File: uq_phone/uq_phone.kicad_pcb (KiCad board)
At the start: 4 copper layers, 116.9 x 105 mm, 171 parts, among them J1 USB4105-GF-A, J10 Conn_01x02, J11 FTSH-105-XX-X-DV, J2 S3B-PH-SM4-TB_LF__SN_, J3 20279-001E-03, J4 20279-001E-03, J5 KP15B-6S-SF_800_, J7 Conn_01x02, J8 541324562, J9 SJ-3551B-MSMT-TR-67, Q1 MMBT3904, Q2 MMBT3904, U1 MCP73871-2CCI_ML, U10 TS3A5018RSVR, U11 NAU88C22YG, U12 MCP1664T-E/OT, U13 TPD3F303DQDR, U14 TPD8F003DQDR, U2 TPS62162DSGR, U3 BQ27441DRZR-G1A, U4 RC7620_1104625, U5 TXB0108RGYR, U6 TXB0108RGYR, U7 STM32H730VBTx, U8 LSM6DSVTR, U9 DRV2603RUNR

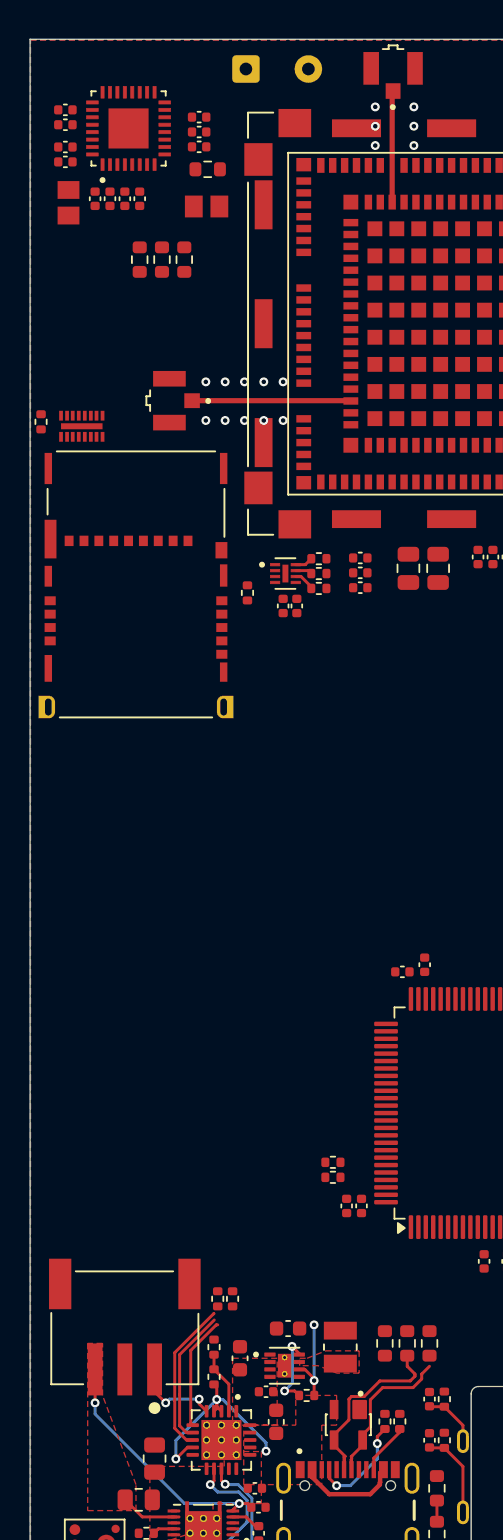
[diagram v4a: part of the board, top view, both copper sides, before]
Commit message: Update display
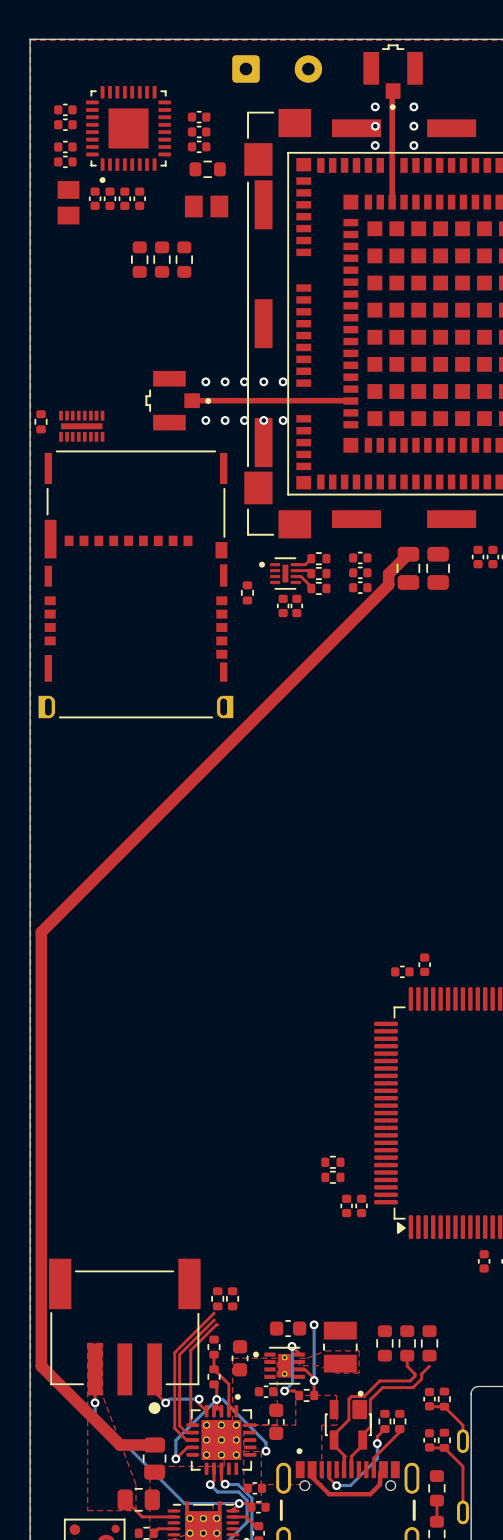
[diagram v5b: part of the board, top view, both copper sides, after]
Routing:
- net +VMOB: track 0.00 -> 74.7 mm

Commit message: Arrange PCB
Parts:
- removed R52, R53: 0R, Resistor_SMD:R_0603_1608Metric
- J7: footprint Connector_Wire:SolderWire-0.25sqmm_1x02_P4.2mm_D0.65mm_OD1.7mm -> Connector_Wire:SolderWire-0.15sqmm_1x02_P4mm_D0.5mm_OD1.5mm
- moved Q2 57.7 mm to (30.3, 104.2), turned to 180 degrees
- moved R17 53.0 mm to (33.0, 105.2), turned to -90 degrees
- moved R18 51.9 mm to (33.0, 103.2), turned to -90 degrees
- moved R19 51.7 mm to (43.2, 103.3)
- moved R20 51.7 mm to (40.2, 103.3)
- moved R21 51.7 mm to (44.7, 103.3)
- moved R22 51.7 mm to (41.7, 103.3)
- moved R12 50.5 mm to (38.5, 105.2)
- moved R13 50.5 mm to (38.5, 103.2)
- moved Q1 50.4 mm to (35.8, 104.2)
- moved R32 47.6 mm to (65.7, 123.2), turned to 0 degrees
- moved U14 43.2 mm to (64.9, 120.9), turned to 90 degrees
- moved C41 42.5 mm to (66.1, 98.6), turned to 90 degrees
- moved C44 42.0 mm to (64.0, 98.3), turned to 0 degrees
- moved C45 41.1 mm to (62.1, 98.3)
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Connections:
- U11 pad 16: Net-(U11-SCLK) -> AUD_SCL
- U11 pad 17: Net-(U11-SDIO) -> AUD_SDA
- U4 pad P14: GND -> (no net)
- U4 pad P17: GND -> (no net)
- U7 pad 91: MOB_RST -> MOB_RST_CTL
- U7 pad 93: MOB_PWR -> unconnected-(U7-PB7-Pad93)
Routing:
- net +VMOB: track 74.7 -> 0.00 mm
- net Net-(U11-VDDB): track 0.00 -> 14.8 mm, vias 0 -> 2
- net USB_P: track 13.1 -> 3.22 mm
- net USB_N: track 11.3 -> 3.22 mm
- net MOB_SYS_CLK: track 0.00 -> 7.51 mm, vias 0 -> 2
- net Net-(U11-VDDA): track 0.00 -> 3.58 mm
- net Net-(U11-MCLK): track 0.00 -> 3.07 mm
- net Net-(Q1-B): track 0.00 -> 2.80 mm
- net Net-(U11-RMICN): track 0.00 -> 2.44 mm
- net MOB_MAIN_ANT: track 10.7 -> 8.40 mm
- net MIC_OUT: track 0.00 -> 1.57 mm
- net MIC_GND: track 0.00 -> 1.31 mm
- net HP_MIC: track 0.00 -> 1.31 mm
- net VBAT: vias 0 -> 3
- net GND: vias 16 -> 34
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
